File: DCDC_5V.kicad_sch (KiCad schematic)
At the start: 10 parts, among them U10 TPS563200

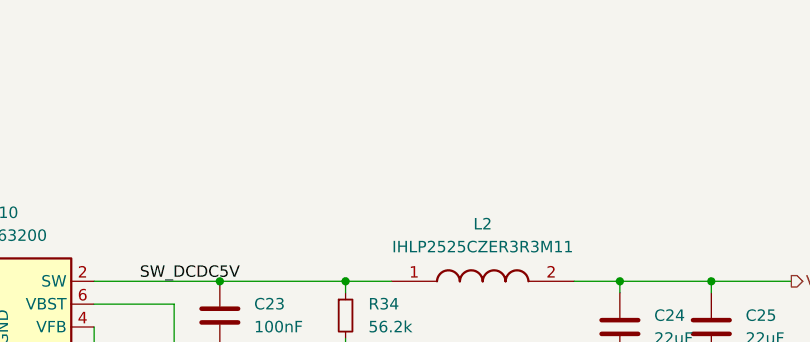
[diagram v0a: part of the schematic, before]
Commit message: add power status LEDs
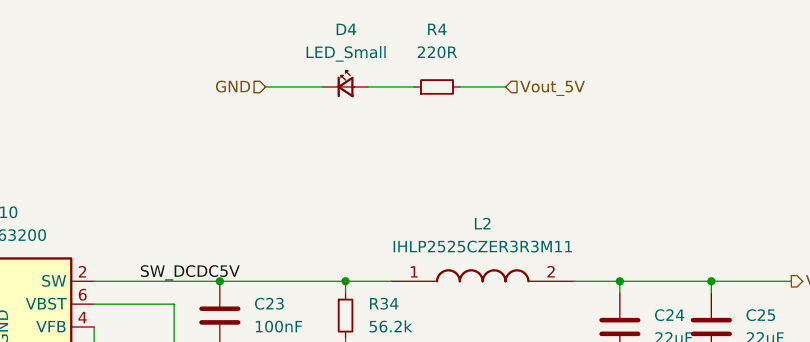
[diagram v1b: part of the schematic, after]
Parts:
- added D4: LED_Small, LED_SMD:LED_0805_2012Metric, symbol Device:LED_Small
- added R4: 220R, Resistor_SMD:R_0603_1608Metric, symbol Device:R_Small
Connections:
- net GND: now also D4.1 (K)
- net Vout_5V: now also R4.2
- new net: D4.2 (A), R4.1
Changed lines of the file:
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@@
+	(wire
+		(pts
+			(xy 170.18 53.34) (xy 175.26 53.34)
+		)
+		(stroke
+			(width 0)
+			(type default)
+		)
+	)
 	(wire
 		(pts
@@
 		(pts
 			(xy 182.88 74.93) (xy 187.96 74.93)
+		)
+		(stroke
+			(width 0)
+			(type default)
+		)
+	)
+	(wire
+		(pts
+			(xy 160.02 53.34) (xy 165.1 53.34)
+		)
+		(stroke
+			(width 0)
+			(type default)
+		)
+	)
+	(wire
+		(pts
+			(xy 148.59 53.34) (xy 154.94 53.34)
 		)
 		(stroke
@@
 		)
 	)
+	(hierarchical_label "Vout_5V"
+		(shape input)
+		(at 175.26 53.34 0)
+		(fields_autoplaced yes)
+		(effects
+			(font
+				(size 1.27 1.27)
+			)
+			(justify left)
+		)
+	)
 	(hierarchical_label "GND"
 		(shape input)
@@
 			)
 			(justify left)
+		)
+	)
+	(hierarchical_label "GND"
+		(shape input)
+		(at 148.59 53.34 180)
+		(fields_autoplaced yes)
+		(effects
+			(font
+				(size 1.27 1.27)
+			)
+			(justify right)
 		)
 	)
@@
 					(unit 1)
 				)
+			)
+		)
+	)
+	(symbol
+		(lib_id "Device:LED_Small")
+		(at 157.48 53.34 0)
+		(unit 1)
+		(exclude_from_sim no)
+		(in_bom yes)
+		(on_board yes)
+		(dnp no)
+		(fields_autoplaced yes)
+		(property "Reference" "D4"
+			(at 157.5435 46.99 0)
+			(effects
+				(font
+					(size 1.27 1.27)
+				)
+			)
+		)
+		(property "Value" "LED_Small"
+			(at 157.5435 49.53 0)
+			(effects
+				(font
+					(size 1.27 1.27)
+				)
+			)
+		)
+		(property "Footprint" "LED_SMD:LED_0805_2012Metric"
+			(at 157.48 53.34 90)
+			(effects
+				(font
+					(size 1.27 1.27)
+				)
+				(hide yes)
+			)
+		)
+		(property "Datasheet" "~"
+			(at 157.48 53.34 90)
+			(effects
+				(font
+					(size 1.27 1.27)
+				)
+				(hide yes)
+			)
+		)
+		(property "Description" ""
+			(at 157.48 53.34 0)
+			(effects
+				(font
+					(size 1.27 1.27)
+				)
+				(hide yes)
+			)
+		)
+		(pin "1"
+		)
+		(pin "2"
+		)
+		(instances
+			(project "carte_servo"
+				(path "/e63e39d7-6ac0-4ffd-8aa3-1841a4541b55/aa21c943-be8f-4f59-86c0-b8fbf57c2a51"
+					(reference "D4")
+					(unit 1)
+				)
+			)
+		)
+	)
+	(symbol
+		(lib_id "Device:R_Small")
+		(at 167.64 53.34 90)
+		(unit 1)
+		(exclude_from_sim no)
+		(in_bom yes)
+		(on_board yes)
+		(dnp no)
+		(fields_autoplaced yes)
+		(property "Reference" "R4"
+			(at 167.64 46.99 90)
+			(effects
+				(font
+					(size 1.27 1.27)
+				)
+			)
+		)
+		(property "Value" "220R"
+			(at 167.64 49.53 90)
+			(effects
+				(font
+					(size 1.27 1.27)
+				)
+			)
+		)
+		(property "Footprint" "Resistor_SMD:R_0603_1608Metric"
+			(at 167.64 53.34 0)
+			(effects
+				(font
+					(size 1.27 1.27)
+				)
+				(hide yes)
+			)
+		)
+		(property "Datasheet" "~"
+			(at 167.64 53.34 0)
+			(effects
+				(font
+					(size 1.27 1.27)
+				)
+				(hide yes)
+			)
+		)
+		(property "Description" ""
+			(at 167.64 53.34 0)
+			(effects
+				(font
+					(size 1.27 1.27)
+				)
+				(hide yes)
+			)
+		)
+		(pin "1"
+		)
+		(pin "2"
+		)
+		(instances
+			(project "carte_servo"
+				(path "/e63e39d7-6ac0-4ffd-8aa3-1841a4541b55/aa21c943-be8f-4f59-86c0-b8fbf57c2a51"
+					(reference "R4")
+					(unit 1)
+				)

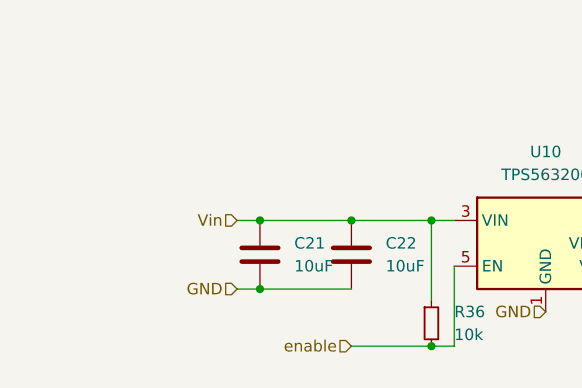
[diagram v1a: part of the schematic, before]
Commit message: 12V logic for ESP32 + add legends + fine tune
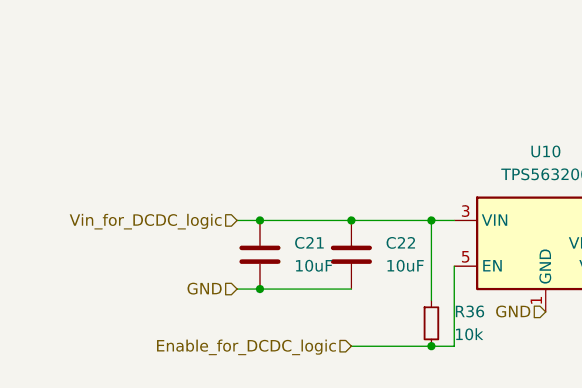
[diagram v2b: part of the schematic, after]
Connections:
- net Vin renamed Vin_for_DCDC_logic
- net enable renamed Enable_for_DCDC_logic
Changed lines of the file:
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@@
 		)
 	)
-	(hierarchical_label "Vin"
+	(hierarchical_label "Vin_for_DCDC_logic"
 		(shape input)
 		(at 85.09 74.93 180)
@@
 		)
 	)
-	(hierarchical_label "enable"
+	(hierarchical_label "Enable_for_DCDC_logic"
 		(shape input)
 		(at 97.79 88.9 180)

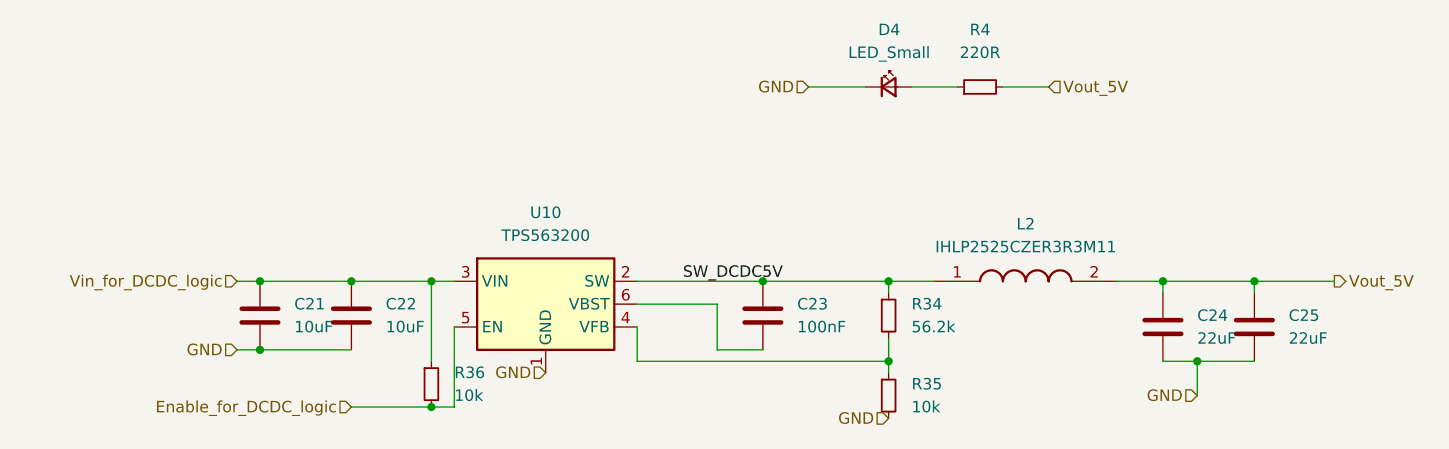
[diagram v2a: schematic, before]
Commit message: fix DCDC5V schematic
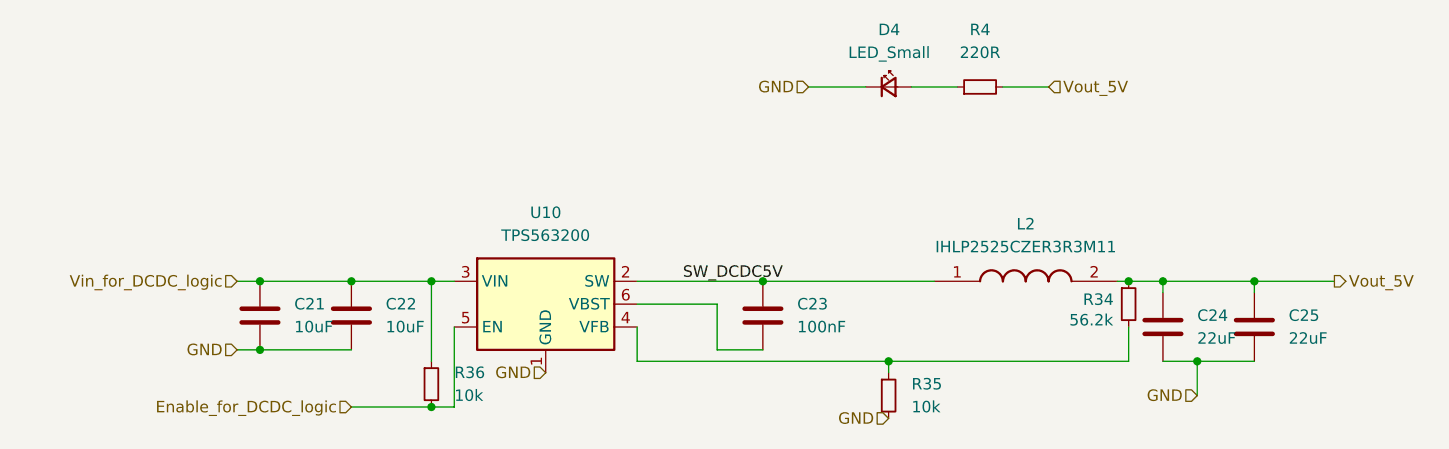
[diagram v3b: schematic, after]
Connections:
- net SW_DCDC5V: no longer R34.1
- net Vout_5V: now also R34.1
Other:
- moved on the sheet: R34
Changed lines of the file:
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@@
 	)
 	(junction
-		(at 157.48 74.93)
+		(at 184.15 74.93)
 		(diameter 0)
 		(color 0 0 0 0)
@@
 	(wire
 		(pts
-			(xy 143.51 74.93) (xy 157.48 74.93)
+			(xy 143.51 74.93) (xy 162.56 74.93)
 		)
 		(stroke
@@
 	(wire
 		(pts
-			(xy 157.48 76.2) (xy 157.48 74.93)
-		)
-		(stroke
-			(width 0)
-			(type default)
-		)
-	)
-	(wire
-		(pts
 			(xy 87.63 74.93) (xy 97.79 74.93)
 		)
@@
 	(wire
 		(pts
-			(xy 182.88 74.93) (xy 187.96 74.93)
+			(xy 182.88 74.93) (xy 184.15 74.93)
+		)
+		(stroke
+			(width 0)
+			(type default)
+		)
+	)
+	(wire
+		(pts
+			(xy 184.15 74.93) (xy 187.96 74.93)
 		)
 		(stroke
@@
 	(wire
 		(pts
-			(xy 162.56 74.93) (xy 157.48 74.93)
-		)
-		(stroke
-			(width 0)
-			(type default)
-		)
-	)
-	(wire
-		(pts
 			(xy 129.54 77.47) (xy 138.43 77.47)
 		)
@@
 	(wire
 		(pts
-			(xy 157.48 81.28) (xy 157.48 83.82)
+			(xy 184.15 80.01) (xy 184.15 83.82)
 		)
 		(stroke
@@
 		(pts
 			(xy 138.43 82.55) (xy 143.51 82.55)
+		)
+		(stroke
+			(width 0)
+			(type default)
+		)
+	)
+	(wire
+		(pts
+			(xy 184.15 83.82) (xy 157.48 83.82)
 		)
 		(stroke
@@
 	(symbol
 		(lib_id "Device:R_Small")
-		(at 157.48 78.74 0)
+		(at 184.15 77.47 0)
 		(unit 1)
 		(exclude_from_sim no)
@@
 		(on_board yes)
 		(dnp no)
-		(fields_autoplaced yes)
 		(property "Reference" "R34"
-			(at 160.02 77.4699 0)
+			(at 179.07 76.962 0)
 			(effects
 				(font
@@
 		)
 		(property "Value" "56.2k"
-			(at 160.02 80.0099 0)
+			(at 177.546 79.248 0)
 			(effects
 				(font
@@
 		)
 		(property "Footprint" "Capacitor_SMD:C_0603_1608Metric"
-			(at 157.48 78.74 0)
+			(at 184.15 77.47 0)
 			(effects
 				(font
@@
 		)
 		(property "Datasheet" "~"
-			(at 157.48 78.74 0)
+			(at 184.15 77.47 0)
 			(effects
 				(font
@@
 		)
 		(property "Description" "Resistor, small symbol"
-			(at 157.48 78.74 0)
+			(at 184.15 77.47 0)
 			(effects
 				(font

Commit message: Add BOM
Add LCSC reference and correct few footprint acording bom
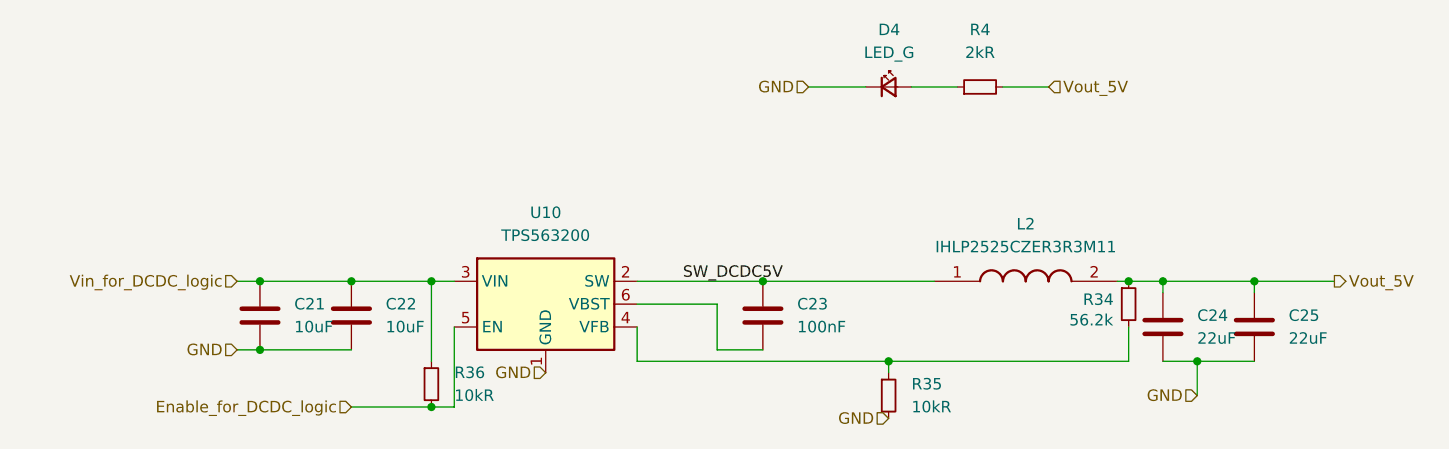
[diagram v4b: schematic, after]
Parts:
- C21, C22: footprint LED_SMD:LED_0805_2012Metric -> Capacitor_SMD:C_0805_2012Metric; LCSC# (none) -> C1713
- C23: LCSC# (none) -> C14663
- C24, C25: LCSC# (none) -> C5674
- D4: value LED_Small -> LED_G; LCSC# (none) -> C965815
- L2: Height 3 -> (none); LCSC# (none) -> C845025; Manufacturer_Name Vishay -> (none); Manufacturer_Part_Number IHLP2525CZER3R3M11 -> (none); Mouser Part Number 70-IHLP2525CZER3R3M1 -> (none); Mouser Price/Stock https://www.mouser.co.uk/ProductDetail/Vishay-Dale/IHLP2525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 -> (none)
- R34: LCSC# (none) -> C2930117
- R35, R36: value 10k -> 10kR; footprint Capacitor_SMD:C_0603_1608Metric -> Resistor_SMD:R_0603_1608Metric; LCSC# (none) -> C2930027
- R4: value 220R -> 2kR; LCSC# (none) -> C2907137
- U10: LCSC# (none) -> C97253
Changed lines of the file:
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@@
 	(label "SW_DCDC5V"
 		(at 134.62 74.93 0)
-		(fields_autoplaced yes)
 		(effects
 			(font
@@
 		(shape input)
 		(at 175.26 53.34 0)
-		(fields_autoplaced yes)
 		(effects
 			(font
@@
 		(shape input)
 		(at 85.09 82.55 180)
-		(fields_autoplaced yes)
 		(effects
 			(font
@@
 		(shape output)
 		(at 207.01 74.93 0)
-		(fields_autoplaced yes)
 		(effects
 			(font
@@
 		(shape input)
 		(at 148.59 53.34 180)
-		(fields_autoplaced yes)
 		(effects
 			(font
@@
 		(shape input)
 		(at 157.48 90.17 180)
-		(fields_autoplaced yes)
 		(effects
 			(font
@@
 		(shape input)
 		(at 191.77 87.63 180)
-		(fields_autoplaced yes)
 		(effects
 			(font
@@
 		(shape input)
 		(at 85.09 74.93 180)
-		(fields_autoplaced yes)
 		(effects
 			(font
@@
 		(shape input)
 		(at 119.38 85.09 180)
-		(fields_autoplaced yes)
 		(effects
 			(font
@@
 		(shape input)
 		(at 97.79 88.9 180)
-		(fields_autoplaced yes)
 		(effects
 			(font
@@
 			)
 		)
+		(property "LCSC#" "C2930117"
+			(at 184.15 77.47 0)
+			(effects
+				(font
+					(size 1.27 1.27)
+				)
+				(hide yes)
+			)
+		)
 		(pin "2"
 		)
@@
 			)
 		)
+		(property "LCSC#" "C5674"
+			(at 187.96 80.01 0)
+			(effects
+				(font
+					(size 1.27 1.27)
+				)
+				(hide yes)
+			)
+		)
 		(pin "2"
 		)
@@
 			)
 		)
-		(property "Value" "10k"
+		(property "Value" "10kR"
 			(at 109.22 87.6299 0)
 			(effects
@@
 			)
 		)
-		(property "Footprint" "Capacitor_SMD:C_0603_1608Metric"
+		(property "Footprint" "Resistor_SMD:R_0603_1608Metric"
 			(at 106.68 86.36 0)
 			(effects
@@
 			)
 		)
+		(property "LCSC#" "C2930027"
+			(at 106.68 86.36 0)
+			(effects
+				(font
+					(size 1.27 1.27)
+				)
+				(hide yes)
+			)
+		)
 		(pin "2"
 		)
@@
 			)
 		)
+		(property "LCSC#" "C97253"
+			(at 119.38 77.47 0)
+			(effects
+				(font
+					(size 1.27 1.27)
+				)
+				(hide yes)
+			)
+		)
 		(pin "3"
 		)
@@
 			)
 		)
-		(property "Height" "3"
-			(at 179.07 471.12 0)
-			(effects
-				(font
-					(size 1.27 1.27)
-				)
-				(justify left top)
-				(hide yes)
-			)
-		)
-		(property "Mouser Part Number" "70-IHLP2525CZER3R3M1"
-			(at 179.07 571.12 0)
-			(effects
-				(font
-					(size 1.27 1.27)
-				)
-				(justify left top)
-				(hide yes)
-			)
-		)
-		(property "Mouser Price/Stock" "https://www.mouser.co.uk/ProductDetail/Vishay-Dale/IHLP2525CZER3R3M11?qs=gMuw6kkpPFg%2FbFUyKU6i8w%3D%3D"
-			(at 179.07 671.12 0)
-			(effects
-				(font
-					(size 1.27 1.27)
-				)
-				(justify left top)
-				(hide yes)
-			)
-		)
-		(property "Manufacturer_Name" "Vishay"
-			(at 179.07 771.12 0)
-			(effects
-				(font
-					(size 1.27 1.27)
-				)
-				(justify left top)
-				(hide yes)
-			)
-		)
-		(property "Manufacturer_Part_Number" "IHLP2525CZER3R3M11"
-			(at 179.07 871.12 0)
-			(effects
-				(font
-					(size 1.27 1.27)
-				)
-				(justify left top)
+		(property "LCSC#" "C845025"
+			(at 162.56 74.93 0)
+			(effects
+				(font
+					(size 1.27 1.27)
+				)
 				(hide yes)
 			)
@@
 			)
 		)
+		(property "LCSC#" "C5674"
+			(at 198.12 80.01 0)
+			(effects
+				(font
+					(size 1.27 1.27)
+				)
+				(hide yes)
+			)
+		)
 		(pin "2"
 		)
@@
 			)
 		)
-		(property "Value" "LED_Small"
+		(property "Value" "LED_G"
 			(at 157.5435 49.53 0)
 			(effects
@@
 			)
 		)
+		(property "LCSC#" "C965815"
+			(at 157.48 53.34 0)
+			(effects
+				(font
+					(size 1.27 1.27)
+				)
+				(hide yes)
+			)
+		)
 		(pin "1"
 		)
@@
 			)
 		)
-		(property "Value" "220R"
+		(property "Value" "2kR"
 			(at 167.64 49.53 90)
 			(effects
@@
 			)
 		)
+		(property "LCSC#" "C2907137"
+			(at 167.64 53.34 0)
+			(effects
+				(font
+					(size 1.27 1.27)
+				)
+				(hide yes)
+			)
+		)
 		(pin "1"
 		)
@@
 			)
 		)
+		(property "LCSC#" "C14663"
+			(at 143.51 78.74 0)
+			(effects
+				(font
+					(size 1.27 1.27)
+				)
+				(hide yes)
+			)
+		)
 		(pin "2"
 		)
@@
 			)
 		)
-		(property "Value" "10k"
+		(property "Value" "10kR"
 			(at 160.02 88.8999 0)
 			(effects
@@
 			)
 		)
-		(property "Footprint" "Capacitor_SMD:C_0603_1608Metric"
+		(property "Footprint" "Resistor_SMD:R_0603_1608Metric"
 			(at 157.48 87.63 0)
 			(effects
@@
 			)
 		)
+		(property "LCSC#" "C2930027"
+			(at 157.48 87.63 0)
+			(effects
+				(font
+					(size 1.27 1.27)
+				)
+				(hide yes)
+			)
+		)
 		(pin "2"
 		)
@@
 			)
 		)
-		(property "Footprint" "LED_SMD:LED_0805_2012Metric"
+		(property "Footprint" "Capacitor_SMD:C_0805_2012Metric"
 			(at 88.5952 82.55 0)
 			(effects
@@
 			)
 		)
+		(property "LCSC#" "C1713"
+			(at 87.63 78.74 0)
+			(effects
+				(font
+					(size 1.27 1.27)
+				)
+				(hide yes)
+			)
+		)
 		(pin "2"
 		)
@@
 			)
 		)
-		(property "Footprint" "LED_SMD:LED_0805_2012Metric"
+		(property "Footprint" "Capacitor_SMD:C_0805_2012Metric"
 			(at 98.7552 82.55 0)
 			(effects
@@
 			(at 97.79 78.74 0)
 			(effects
+				(font
+					(size 1.27 1.27)
+				)
+				(hide yes)
+			)
+		)
+		(property "LCSC#" "C1713"
+			(at 97.79 78.74 0)
+			(effects

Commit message: update to Kicad 9 + small fixes
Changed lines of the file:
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@@
 (kicad_sch
-	(version 20231120)
+	(version 20250114)
 	(generator "eeschema")
-	(generator_version "8.0")
+	(generator_version "9.0")
 	(paper "A4")
 	(junction
@@
 			)
 		)
-		(property "Description" ""
+		(property "Description" "Light emitting diode, small symbol"
 			(at 157.48 53.34 0)
 			(effects
@@
 		)
 		(property "LCSC#" "C965815"
+			(at 157.48 53.34 0)
+			(effects
+				(font
+					(size 1.27 1.27)
+				)
+				(hide yes)
+			)
+		)
+		(property "Sim.Pin" "1=K 2=A"
 			(at 157.48 53.34 0)
 			(effects
@@
 			)
 		)
-		(property "Description" ""
+		(property "Description" "Resistor, small symbol"
 			(at 167.64 53.34 0)
 			(effects

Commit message: update BOM
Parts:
- R34: value 56.2k -> 56.2kR
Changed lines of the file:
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@@
 			)
 		)
-		(property "Value" "56.2k"
+		(property "Value" "56.2kR"
 			(at 177.546 79.248 0)
 			(effects

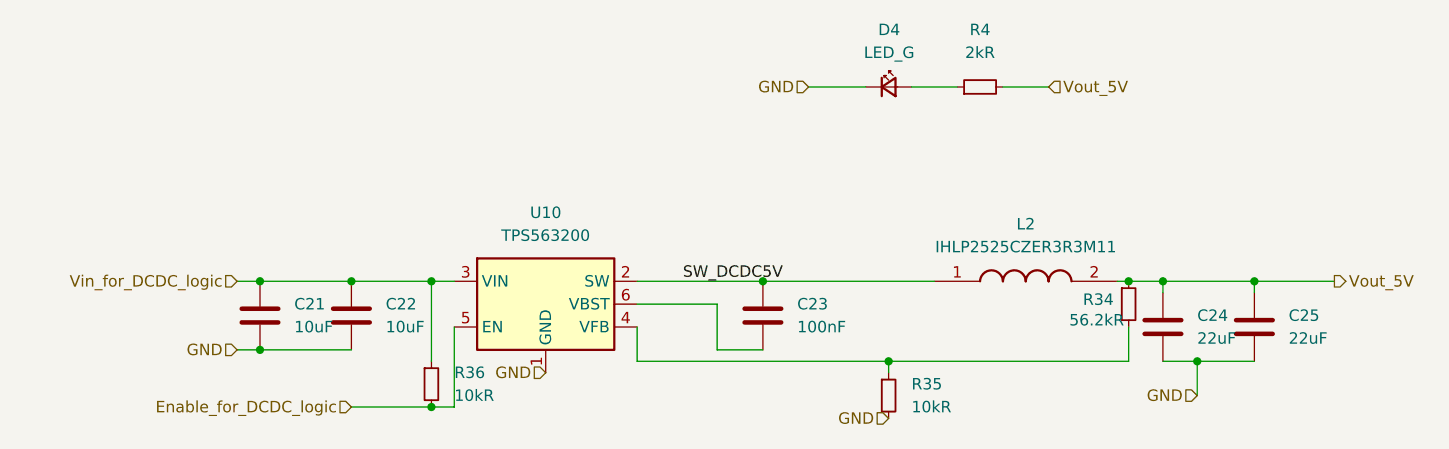
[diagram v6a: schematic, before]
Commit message: update BOM + add big capas (do not take DNP into account)
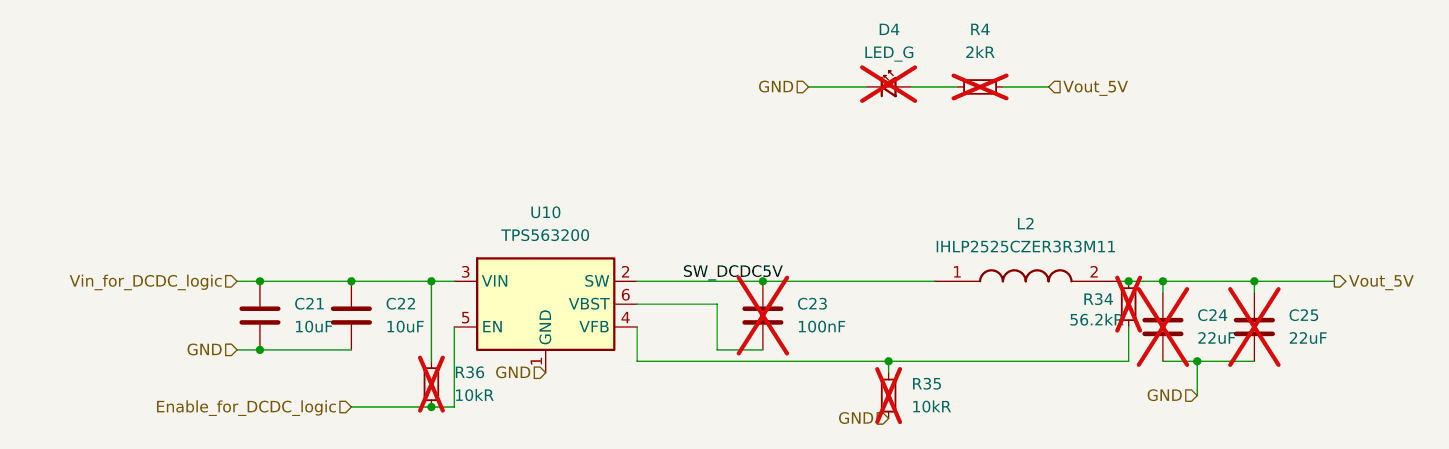
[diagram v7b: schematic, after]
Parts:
- C21, C22: LCSC# C1713 -> C440198
- C23, C24, C25, D4, R34, R35, R36, R4: now not fitted
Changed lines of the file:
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@@
 		(in_bom yes)
 		(on_board yes)
-		(dnp no)
+		(dnp yes)
 		(property "Reference" "R34"
 			(at 179.07 76.962 0)
@@
 		(in_bom yes)
 		(on_board yes)
-		(dnp no)
+		(dnp yes)
 		(fields_autoplaced yes)
 		(property "Reference" "C24"
@@
 		(in_bom yes)
 		(on_board yes)
-		(dnp no)
+		(dnp yes)
 		(fields_autoplaced yes)
 		(property "Reference" "R36"
@@
 		(in_bom yes)
 		(on_board yes)
-		(dnp no)
+		(dnp yes)
 		(fields_autoplaced yes)
 		(property "Reference" "C25"
@@
 		(in_bom yes)
 		(on_board yes)
-		(dnp no)
+		(dnp yes)
 		(fields_autoplaced yes)
 		(property "Reference" "D4"
@@
 		(in_bom yes)
 		(on_board yes)
-		(dnp no)
+		(dnp yes)
 		(fields_autoplaced yes)
 		(property "Reference" "R4"
@@
 		(in_bom yes)
 		(on_board yes)
-		(dnp no)
+		(dnp yes)
 		(fields_autoplaced yes)
 		(property "Reference" "C23"
@@
 		(in_bom yes)
 		(on_board yes)
-		(dnp no)
+		(dnp yes)
 		(fields_autoplaced yes)
 		(property "Reference" "R35"
@@
 			)
 		)
-		(property "LCSC#" "C1713"
+		(property "LCSC#" "C440198"
 			(at 87.63 78.74 0)
 			(effects
@@
 			)
 		)
-		(property "LCSC#" "C1713"
+		(property "LCSC#" "C440198"
 			(at 97.79 78.74 0)
 			(effects
